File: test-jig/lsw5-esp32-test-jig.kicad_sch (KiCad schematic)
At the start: 25 parts, among them J1 Conn_02x03_Odd_Even, J2 Conn_02x05_Odd_Even, J3 Conn_02x03_Odd_Even, J4 Conn_02x05_Odd_Even, J5 USB4105-GF-A, SW1 SW_Push, SW2 SW_Push, U1 LD1117V33, U2 MCP2221AxSL

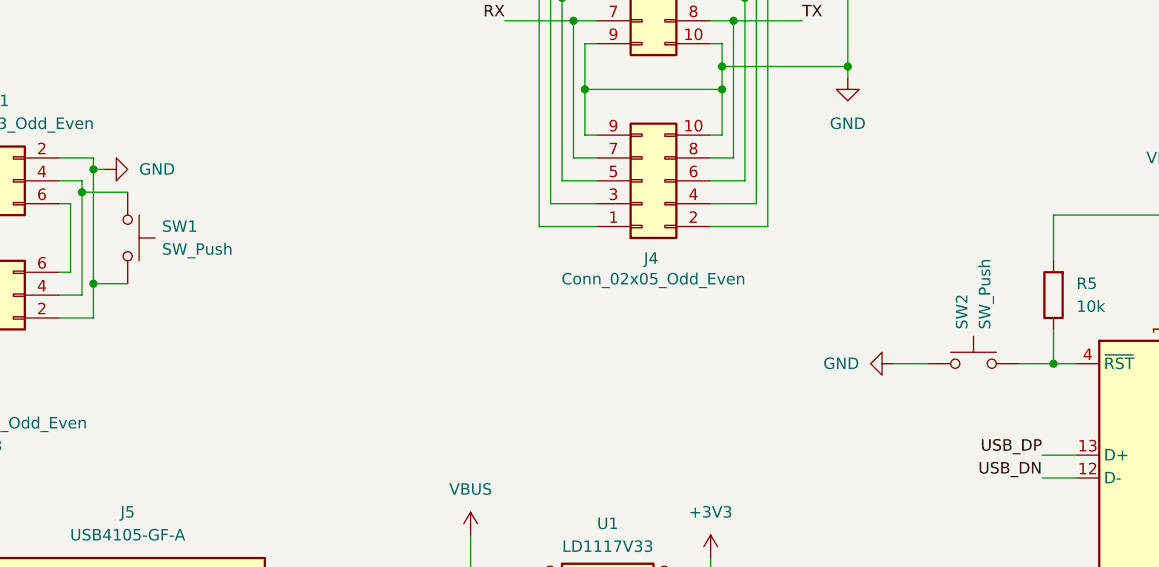
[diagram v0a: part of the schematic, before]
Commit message: test jig: Update button labels on schematic
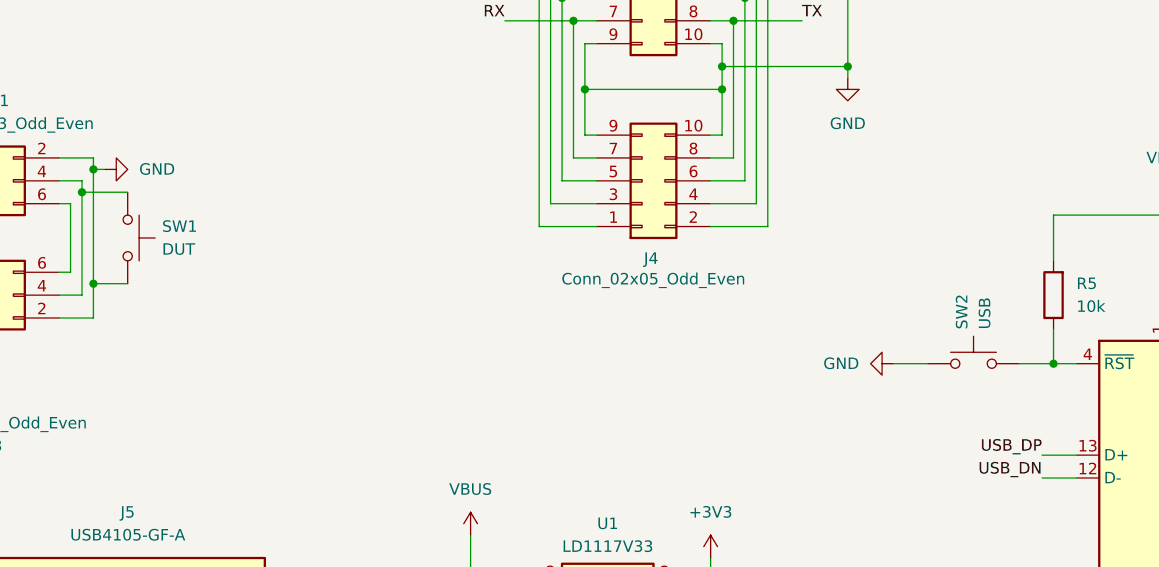
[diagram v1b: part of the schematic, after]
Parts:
- SW1: value SW_Push -> DUT
- SW2: value SW_Push -> USB
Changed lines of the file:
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@@
 			)
 		)
-		(property "Value" "SW_Push"
+		(property "Value" "DUT"
 			(at 102.87 68.5799 90)
 			(effects
@@
 			)
 		)
-		(property "Value" "SW_Push"
+		(property "Value" "USB"
 			(at 194.3099 77.47 90)
 			(effects

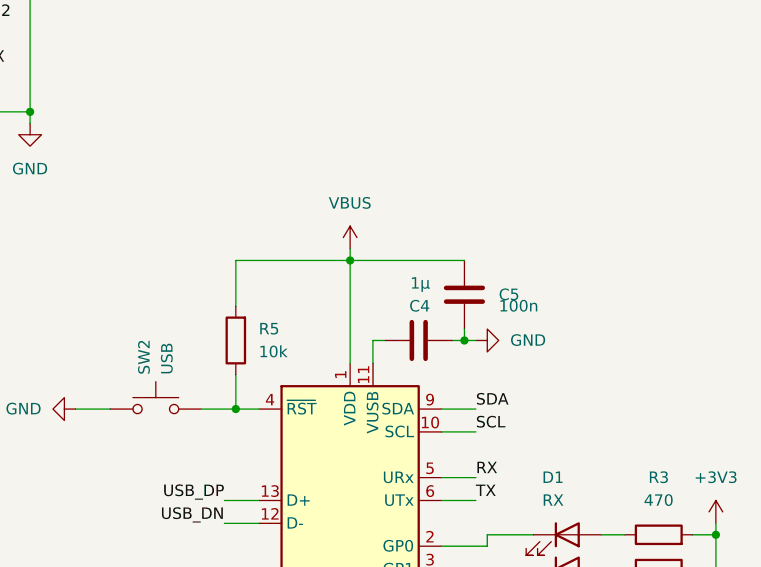
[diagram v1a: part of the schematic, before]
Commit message: test jig: Fix MCP2221A V_USB capacitor value
DS20005565E-page 17

> The VUSB pin requires an external bypass capacitor
> with a value between 0.22 and 0.47 μF (ceramic cap)
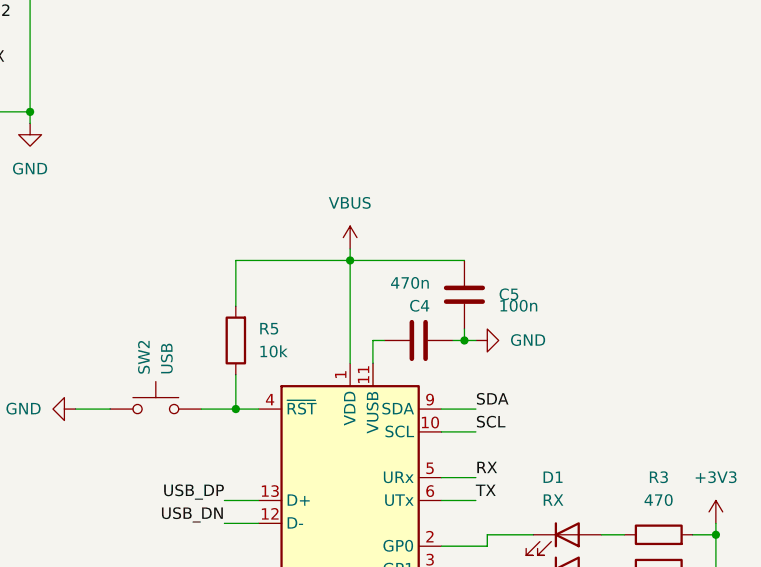
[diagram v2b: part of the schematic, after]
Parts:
- C4: value 1μ -> 470n
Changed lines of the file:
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@@
 			)
 		)
-		(property "Value" "1μ"
+		(property "Value" "470n"
 			(at 223.52 67.3101 90)
 			(effects

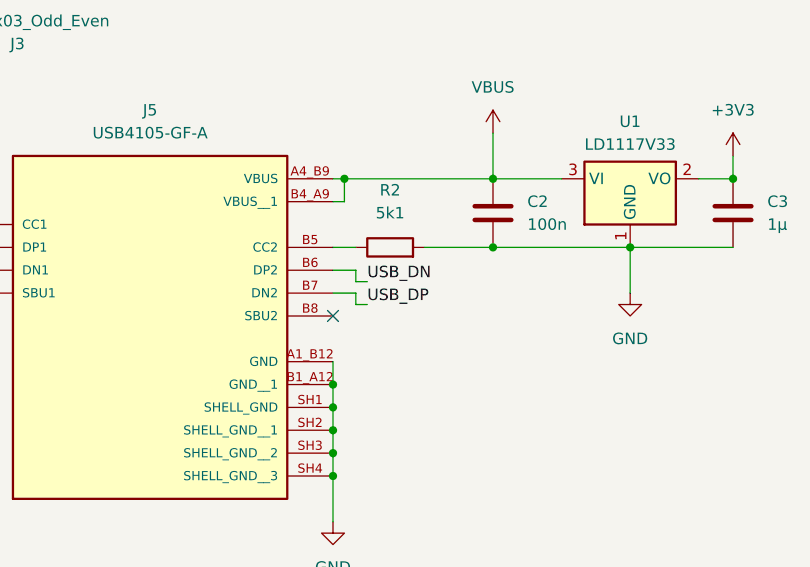
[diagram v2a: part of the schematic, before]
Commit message: test jig: Fix USB only working on one side
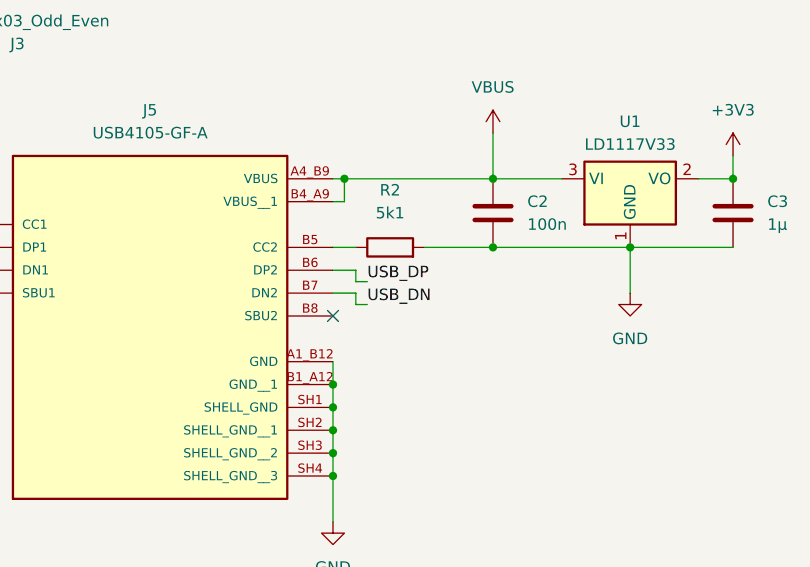
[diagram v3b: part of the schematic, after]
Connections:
- net USB_DN: now also J5.B7 (DN2); no longer J5.B6 (DP2)
- net USB_DP: now also J5.B6 (DP2); no longer J5.B7 (DN2)
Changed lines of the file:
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@@
 	)
 	(label "USB_DN"
-		(at 123.19 116.84 0)
+		(at 123.19 119.38 0)
 		(effects
 			(font
@@
 	)
 	(label "USB_DP"
-		(at 123.19 119.38 0)
+		(at 123.19 116.84 0)
 		(effects
 			(font
